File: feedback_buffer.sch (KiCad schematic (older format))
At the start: 21 parts, among them IC1 DAC53401DSGR, U14 DG412xUE, U15 OPA828, U23 OPA188xxDBV

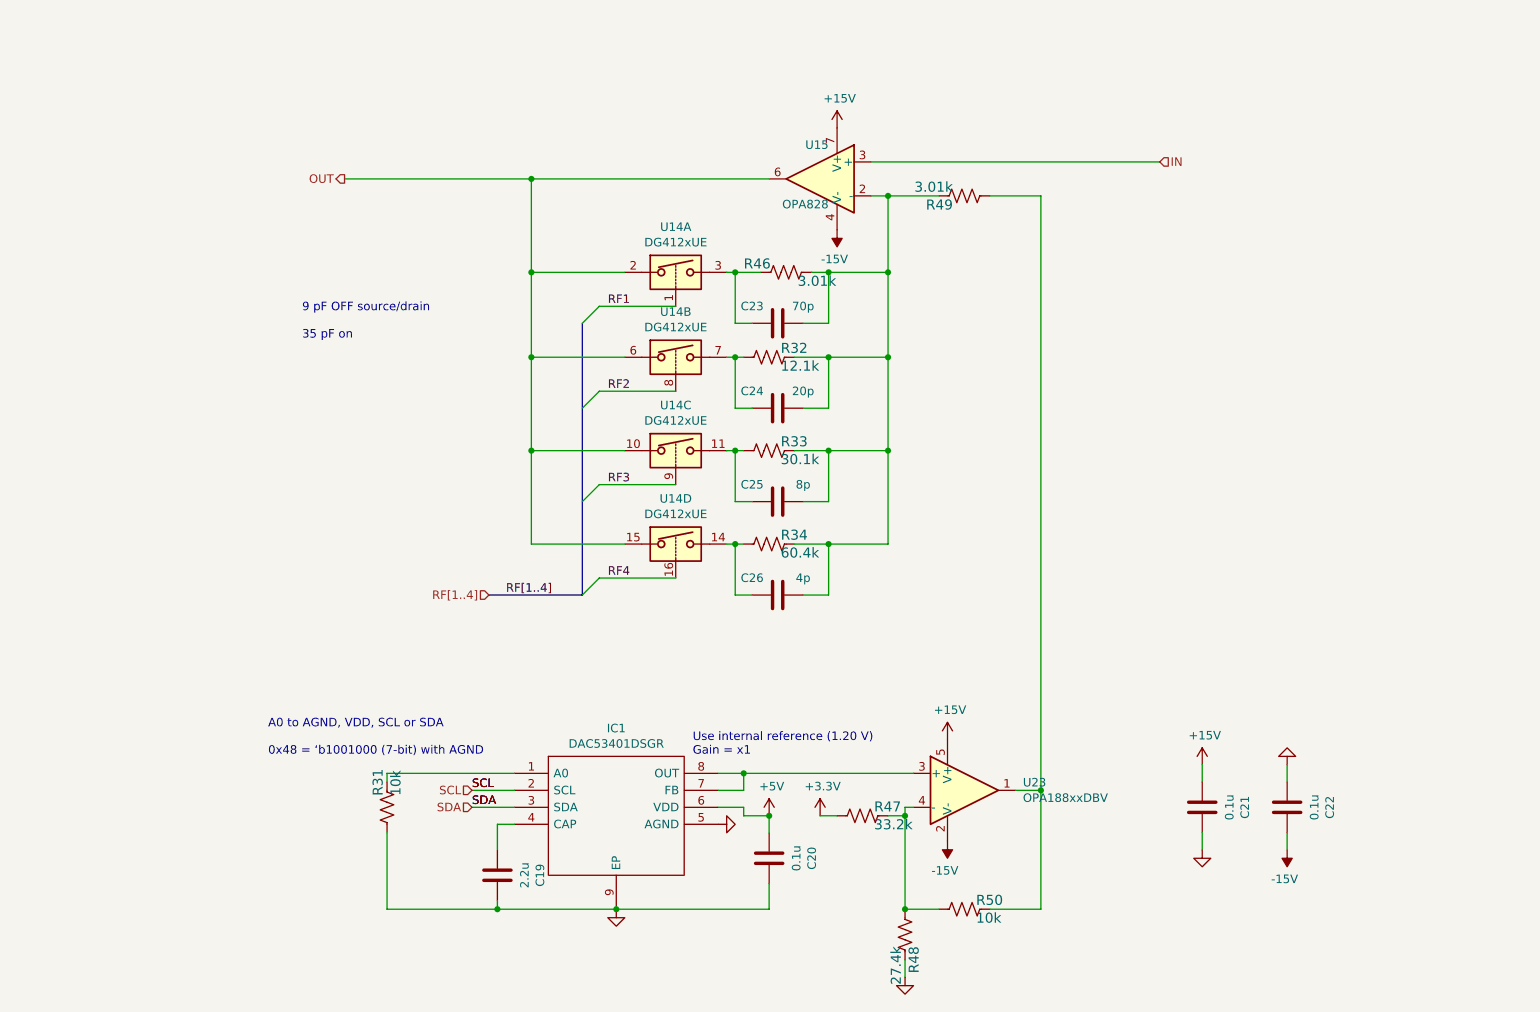
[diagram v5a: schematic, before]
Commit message: updates to README
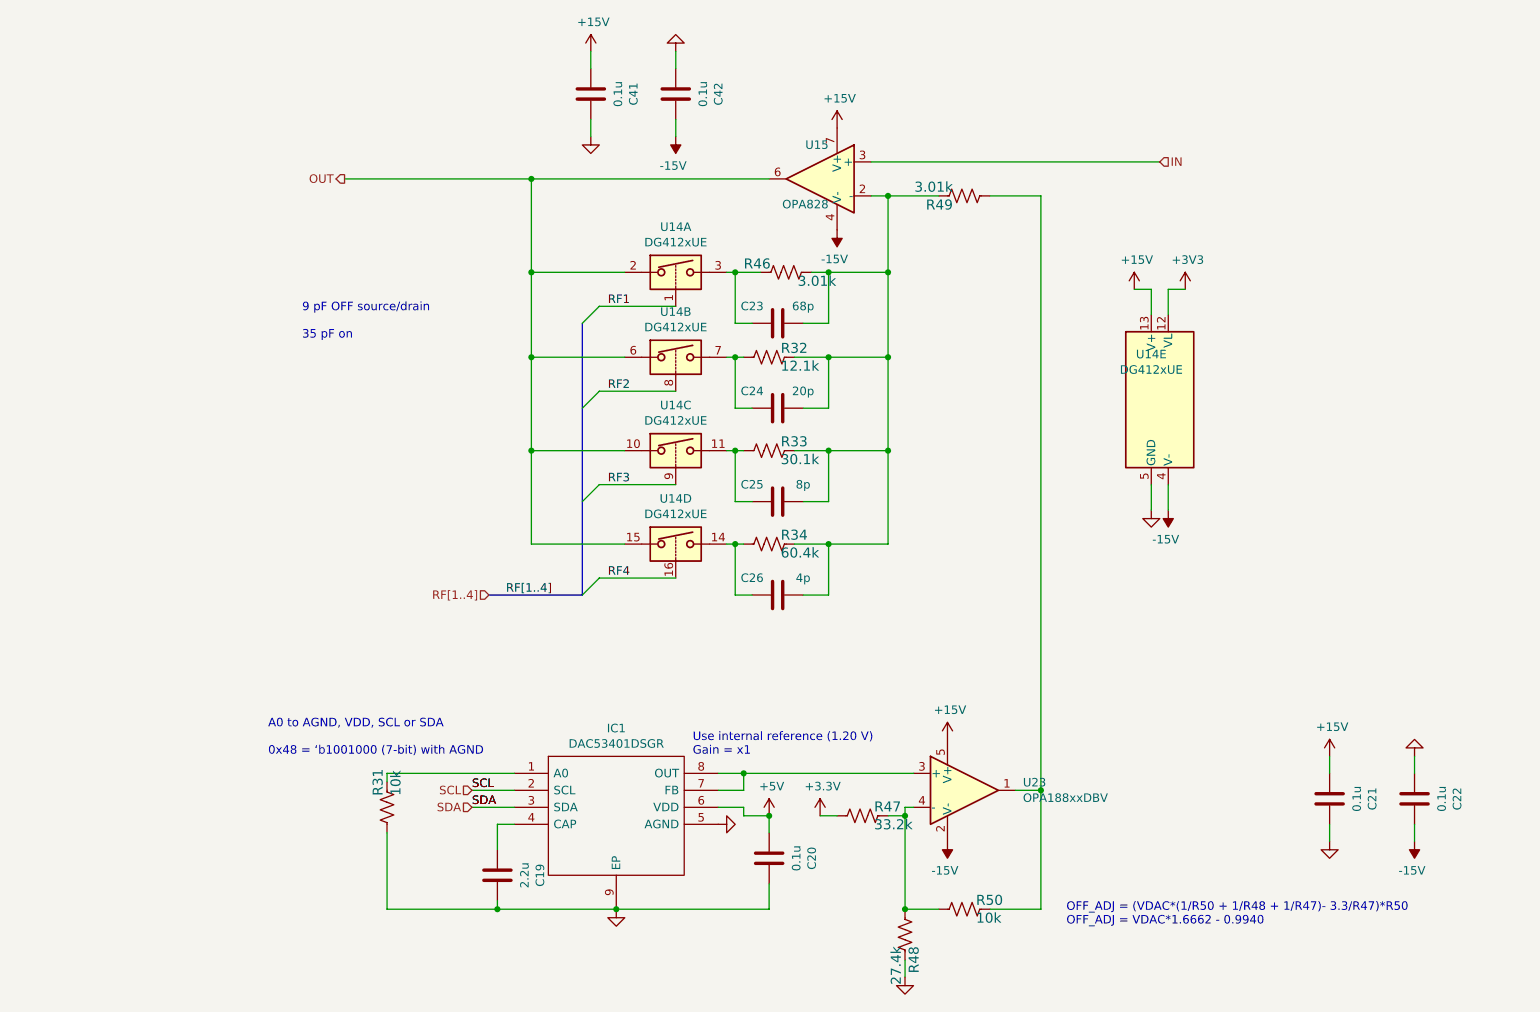
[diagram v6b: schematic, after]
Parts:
- added C41, C42: 0.1u, Capacitor_SMD:C_0603_1608Metric, symbol Device:C
- added unit 5 of U14
- C23: value 70p -> 68p; Manf# (none) -> CC0603KRNPO9BN680
- C24: Manf# (none) -> CC0603JRNPO9BN200
- C25: Manf# (none) -> CC0603CRNPO9BN8R0
- C26: Manf# (none) -> CC0603CRNPO9BN4R0
- U14: Manf# (none) -> DG412CUE+
- U23: Manf# (none) -> OPA188AIDBVR
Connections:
- net +15V: now also C41.2, U14.13 (V+)
- net +3V3: now also U14.12 (VL)
- net -15V: now also C42.1, U14.4 (V-)
- net GND: now also C41.1, C42.2, U14.5 (GND)
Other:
- note added: "OFF_ADJ = (VDAC*(1/R50 + 1/R48 + 1/R47)- 3.3/R47)*R50\nOFF_ADJ = VDAC*1.6662 - 0.9940"
- moved on the sheet: C21, C22

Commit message: readme updates
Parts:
- C19: Manf# CL10B225KP8NNNC -> CL10B225KP8NFNC
- C23: Manf# CC0603KRNPO9BN680 -> CC0603FRNPO0BN680
- C25: Manf# CC0603CRNPO9BN8R0 -> 06031A8R0CAT2A
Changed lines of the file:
@@
 F 2 "Capacitor_SMD:C_0603_1608Metric" H 3938 5450 50  0001 C CNN
 F 3 "~" H 3900 5600 50  0001 C CNN
-F 4 "CL10B225KP8NNNC" H 3648 5700 50  0001 C CNN "Manf#"
+F 4 "CL10B225KP8NFNC" H 3648 5700 50  0001 C CNN "Manf#"
 F 5 "10%" H 3648 5700 50  0001 C CNN "Tolerance"
 F 6 "10V" H 3648 5700 50  0001 C CNN "voltage"
@@
 F 2 "Capacitor_SMD:C_0603_1608Metric" H 5588 2200 50  0001 C CNN
 F 3 "~" H 5550 2350 50  0001 C CNN
-F 4 "CC0603KRNPO9BN680" H 5298 2450 50  0001 C CNN "Manf#"
+F 4 "CC0603FRNPO0BN680" H 5298 2450 50  0001 C CNN "Manf#"
 F 5 "20%" H 5298 2450 50  0001 C CNN "Tolerance"
 F 6 "25V" H 5298 2450 50  0001 C CNN "voltage"
@@
 F 2 "Capacitor_SMD:C_0603_1608Metric" H 5588 3250 50  0001 C CNN
 F 3 "~" H 5550 3400 50  0001 C CNN
-F 4 "CC0603CRNPO9BN8R0" H 5298 3500 50  0001 C CNN "Manf#"
+F 4 "06031A8R0CAT2A" H 5298 3500 50  0001 C CNN "Manf#"
 F 5 "20%" H 5298 3500 50  0001 C CNN "Tolerance"
 F 6 "25V" H 5298 3500 50  0001 C CNN "voltage"
